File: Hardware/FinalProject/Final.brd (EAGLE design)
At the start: 156 x 63 mm, 47 parts, among them IC1 LM2937

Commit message: Changed to SMD caps near TM4C
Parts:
- removed C10: 2.2uf, EE445L:CAP100MIL
- removed C7, C8, C9: 0.1uf, EE445L:CAP100MIL
- added C21: 4.7uF, EE445L:C0603K
- added UART: (no value), EE445L:1X05
- C1, C3: value 0.01uf -> 4.7uF; device EE445L:CAP100MIL -> EE445L:C0603K
- C2: value 0.1uf -> 4.7uF; device EE445L:CAP100MIL -> EE445L:C0603K
- C4: value 0.1uf -> 2.2uF; device EE445L:CAP100MIL -> EE445L:C0603K
- C5: value 0.01uf -> 1uF; device EE445L:CAP100MIL -> EE445L:C0603K
- C6: value 1.0uf -> 0.1uF; device EE445L:CAP100MIL -> EE445L:C0603K
- moved C5 26.1 mm to (35.3, 46.2)
- moved C6 20.3 mm to (37.0, 46.2)
- moved C3 18.2 mm to (54.1, 50.8), turned to 90 degrees
- moved C1 15.9 mm to (46.2, 38.2), turned to 0 degrees
- moved C4 12.3 mm to (54.1, 47.1), turned to 270 degrees
- moved C2 1.49 mm to (53.1, 54.4)
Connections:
- removed net PA0: U$1.17
- removed net PB4: U$1.58
- new net N$5: UART.5
- new net URX: U$1.17, UART.3
- new net UTX: U$1.18, UART.2
- net +3V3: now also C21.1, UART.1; no longer C4.1, C5.1, C6.1
- net GND: now also C21.2, UART.4; no longer C10.2, C7.2, C8.2, C9.2
- net ST7735_TFT_CS_2: now also U$1.58; no longer U$1.18
- net VDDC: now also C4.1, C5.1, C6.1; no longer C10.1, C7.1, C8.1, C9.1
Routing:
- net UTX: track 0.00 -> 23.1 mm, vias 0 -> 1
- net GND: track 52.6 -> 31.6 mm, vias 2 -> 9
- net URX: track 0.00 -> 18.9 mm, vias 0 -> 1
- net ST7735_TFT_CS_2: track 24.6 -> 40.7 mm, vias 0 -> 2
- net VDDC: track 31.9 -> 20.4 mm
- net +3V3: track 439.0 -> 428.7 mm
- net SSI1_MOSI: track 70.7 -> 71.4 mm
- net ST7735_DC: track 101.1 -> 100.5 mm
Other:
- board text added: "3V3"
- board text added: "5V"
- board text added: "GND"
- board text added: "RXD"
- board text added: "TXD"
- board text added: "UTX-2021F007"

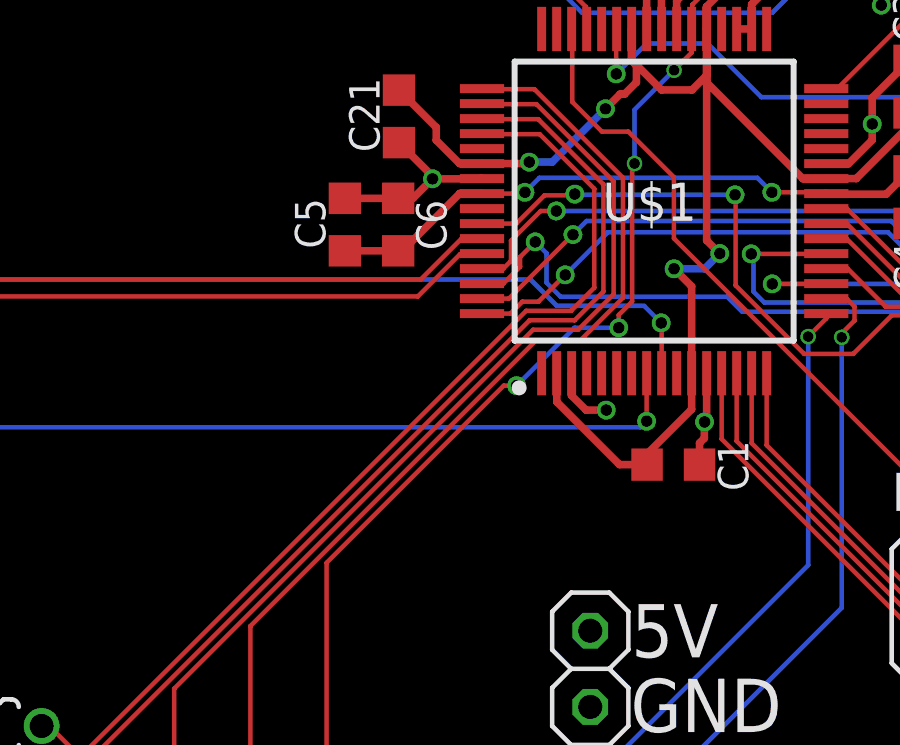
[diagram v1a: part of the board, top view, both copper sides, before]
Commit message: Add lib and fixed cap placement
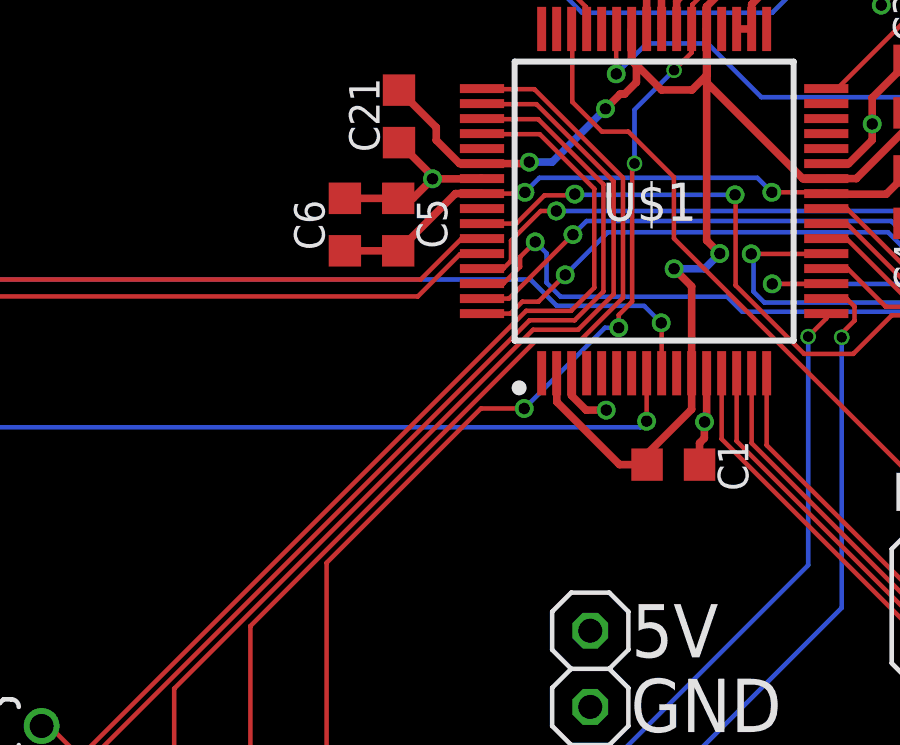
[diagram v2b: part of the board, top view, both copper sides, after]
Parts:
- moved C5 1.78 mm to (37.0, 46.2)
- moved C6 1.78 mm to (35.3, 46.2)
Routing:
- net VDDC: track 20.4 -> 21.2 mm
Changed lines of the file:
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@@
 <attribute name="NAME" x="53.5582" y="45.6056" size="1.016" layer="25" rot="R270"/>
 </element>
-<element name="C5" library="EE445L" package="C0603K" value="1uF" x="35.2552" y="46.1772" smashed="yes" rot="R90">
-<attribute name="NAME" x="34.6052" y="45.3772" size="1.016" layer="25" rot="R90"/>
+<element name="C5" library="EE445L" package="C0603K" value="1uF" x="37.0332" y="46.1772" smashed="yes" rot="R90">
+<attribute name="NAME" x="38.6692" y="45.3772" size="1.016" layer="25" rot="R90"/>
 </element>
-<element name="C6" library="EE445L" package="C0603K" value="0.1uF" x="37.0332" y="46.1772" smashed="yes" rot="R90">
-<attribute name="NAME" x="38.6438" y="45.3264" size="1.016" layer="25" rot="R90"/>
+<element name="C6" library="EE445L" package="C0603K" value="0.1uF" x="35.2552" y="46.1772" smashed="yes" rot="R90">
+<attribute name="NAME" x="34.5798" y="45.3264" size="1.016" layer="25" rot="R90"/>
 </element>
 <element name="UART" library="EE445L" package="1X05" value="" x="43.434" y="27.559" smashed="yes" rot="R90">
@@
 <wire x1="39.7983" y1="47.7265" x2="39.8204" y2="47.7044" width="0.254" layer="1"/>
 <wire x1="51.3076" y1="48.2044" x2="51.302" y2="48.21" width="0.254" layer="1"/>
-<wire x1="35.2552" y1="47.0522" x2="37.0332" y2="47.0522" width="0.254" layer="1"/>
-<wire x1="37.0332" y1="47.0522" x2="37.5272" y2="47.0522" width="0.254" layer="1"/>
-<wire x1="37.5272" y1="47.0522" x2="38.1762" y2="47.7012" width="0.254" layer="1"/>
 <via x="38.1762" y="47.7012" extent="1-16" drill="0.381" diameter="0.635"/>
 <wire x1="38.1762" y1="47.7012" x2="39.773" y2="47.7012" width="0.254" layer="1"/>
@@
 <via x="55.372" y="51.816" extent="1-16" drill="0.381" diameter="0.635"/>
 <contactref element="UART" pad="4"/>
+<wire x1="35.2552" y1="47.0522" x2="37.0332" y2="47.0522" width="0.254" layer="1"/>
+<wire x1="37.0332" y1="47.0522" x2="37.5272" y2="47.0522" width="0.254" layer="1"/>
+<wire x1="37.5272" y1="47.0522" x2="38.1762" y2="47.7012" width="0.254" layer="1"/>
+<wire x1="15.374" y1="44.69" x2="11.564" y2="52.42" width="0" layer="19" extent="1-1"/>
 </signal>
 <signal name="+3V3">
@@
 <wire x1="51.295" y1="47.231" x2="51.316" y2="47.21" width="0.1524" layer="1"/>
 <wire x1="51.3358" y1="47.1902" x2="51.295" y2="47.231" width="0.254" layer="1"/>
-<wire x1="35.2552" y1="45.3022" x2="37.0332" y2="45.3022" width="0.254" layer="1"/>
 <wire x1="39.826" y1="47.21" x2="39.8204" y2="47.2156" width="0.254" layer="1"/>
 <wire x1="39.8204" y1="47.2156" x2="39.0848875" y2="47.2156" width="0.254" layer="1"/>
-<wire x1="37.0332" y1="45.3022" x2="37.1714875" y2="45.3022" width="0.254" layer="1"/>
-<wire x1="37.1714875" y1="45.3022" x2="39.0848875" y2="47.2156" width="0.254" layer="1"/>
 <wire x1="54.0766" y1="47.9666" x2="53.3002" y2="47.1902" width="0.254" layer="1"/>
 <wire x1="53.3002" y1="47.1902" x2="51.3358" y2="47.1902" width="0.254" layer="1"/>
+<wire x1="38.941" y1="47.21" x2="39.826" y2="47.21" width="0.254" layer="1"/>
+<wire x1="35.2552" y1="45.3022" x2="37.0332" y2="45.3022" width="0.254" layer="1"/>
+<wire x1="37.0332" y1="45.3022" x2="38.941" y2="47.21" width="0.254" layer="1"/>
 </signal>
 <signal name="TCK">
@@
 <contactref element="JP3" pad="2"/>
 <wire x1="34.6456" y1="22.479" x2="34.6456" y2="34.90274375" width="0.1524" layer="1"/>
-<wire x1="40.55188125" y1="40.809025" x2="40.978975" y2="40.809025" width="0.1524" layer="1"/>
-<via x="40.978975" y="40.809025" extent="1-16" drill="0.381" diameter="0.635"/>
-<wire x1="40.978975" y1="40.809025" x2="42.907875" y2="42.737925" width="0.1524" layer="16"/>
-<wire x1="42.907875" y1="42.737925" x2="44.384075" y2="42.737925" width="0.1524" layer="16"/>
+<wire x1="39.78988125" y1="40.047025" x2="41.232975" y2="40.047025" width="0.1524" layer="1"/>
+<via x="41.232975" y="40.047025" extent="1-16" drill="0.381" diameter="0.635"/>
+<wire x1="41.232975" y1="40.047025" x2="43.923875" y2="42.737925" width="0.1524" layer="16"/>
+<wire x1="43.923875" y1="42.737925" x2="44.384075" y2="42.737925" width="0.1524" layer="16"/>
 <via x="44.384075" y="42.737925" extent="1-16" drill="0.381" diameter="0.635"/>
-<wire x1="34.6456" y1="34.90274375" x2="40.55188125" y2="40.809025" width="0.1524" layer="1"/>
+<wire x1="34.6456" y1="34.90274375" x2="39.78988125" y2="40.047025" width="0.1524" layer="1"/>
 <via x="44.909925" y="48.211925" extent="1-16" drill="0.35"/>
 <wire x1="44.384075" y1="42.737925" x2="44.384075" y2="43.16501875" width="0.1524" layer="1"/>
